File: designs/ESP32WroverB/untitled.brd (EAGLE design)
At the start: 37 x 48 mm, 19 parts, among them IC6 ESP32-WROVER-B

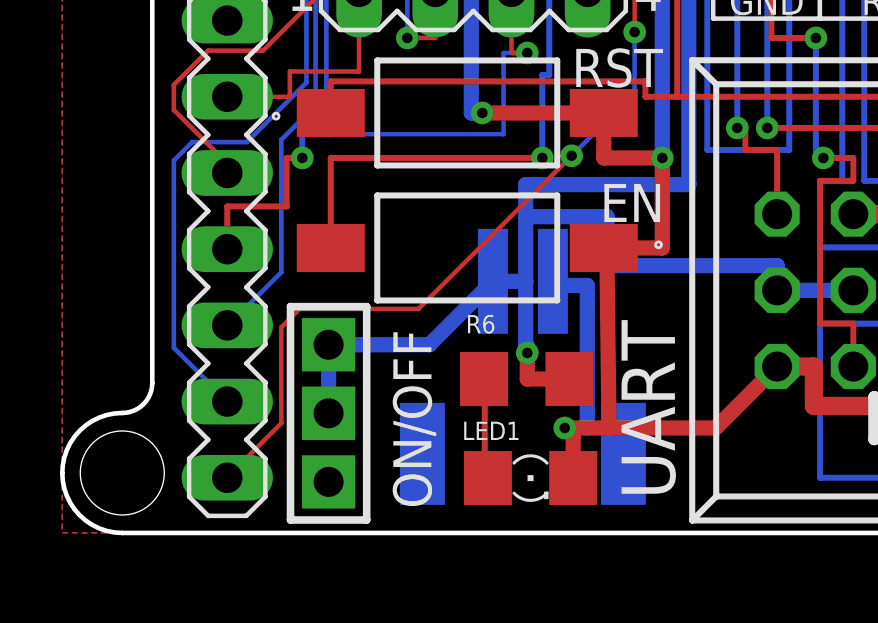
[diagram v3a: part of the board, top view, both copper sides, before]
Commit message: corrected ESP32 on/off error
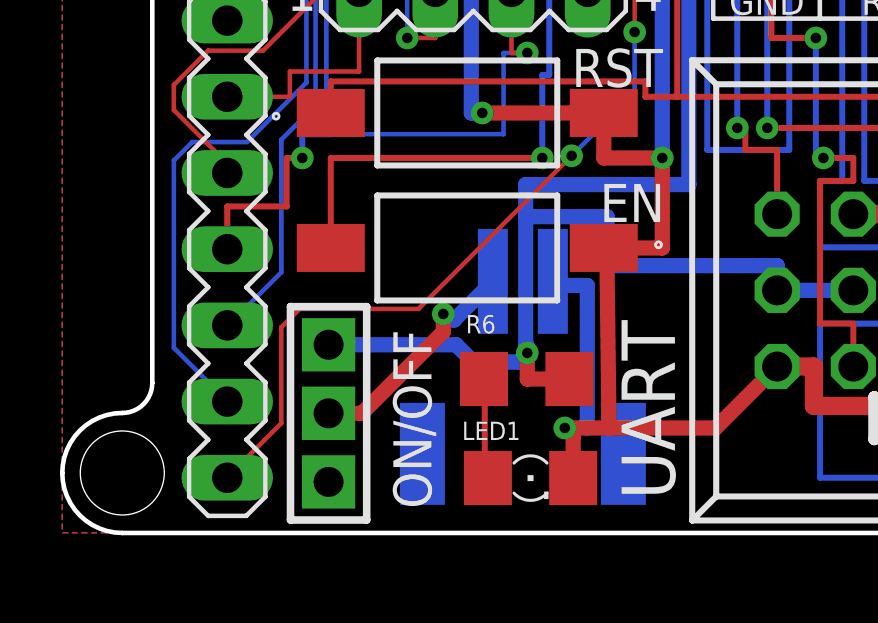
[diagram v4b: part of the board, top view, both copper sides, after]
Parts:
- C1, C4: value (none) -> 1nF
- C2: value (none) -> 100uF
- C3: value (none) -> 1uF
- R1: value 10k -> 12k
- R2: value (none) -> 460ohm
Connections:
- new net N$1: ON/OFF.P$2, POWER.2
- net 3.3V: no longer ON/OFF.P$2, POWER.2
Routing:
- net N$1: track 0.00 -> 7.87 mm, vias 0 -> 1
- net 3.3V: track 99.3 -> 96.6 mm
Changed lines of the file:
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@@
 </autorouter>
 <elements>
-<element name="C1" library="CommonParts" package="C0805" package3d_urn="urn:adsk.eagle:package:23617/2" value="" x="12.584" y="34.087" smashed="yes" rot="MR0">
+<element name="C1" library="CommonParts" package="C0805" package3d_urn="urn:adsk.eagle:package:23617/2" value="1nF" x="12.584" y="34.087" smashed="yes" rot="MR0">
 <attribute name="NAME" x="15.124" y="32.817" size="1.27" layer="26" rot="MR180"/>
 <attribute name="POPULARITY" value="88" x="-2.656" y="-14.173" size="1.778" layer="28" rot="MR0" display="off"/>
@@
 <attribute name="VALUE" x="13.854" y="31.547" size="1.27" layer="28" rot="MR0"/>
 </element>
-<element name="C2" library="CommonParts" package="C0805" package3d_urn="urn:adsk.eagle:package:23617/2" value="" x="12.584" y="31.547" smashed="yes" rot="MR0">
+<element name="C2" library="CommonParts" package="C0805" package3d_urn="urn:adsk.eagle:package:23617/2" value="100uF" x="12.584" y="31.547" smashed="yes" rot="MR0">
 <attribute name="NAME" x="15.124" y="30.277" size="1.27" layer="26" rot="MR180"/>
 <attribute name="POPULARITY" value="88" x="-7.736" y="-16.713" size="1.778" layer="28" rot="MR0" display="off"/>
@@
 <attribute name="VALUE" x="13.854" y="29.007" size="1.27" layer="28" rot="MR0"/>
 </element>
-<element name="C3" library="CommonParts" package="C0805" package3d_urn="urn:adsk.eagle:package:23617/2" value="" x="12.584" y="29.007" smashed="yes" rot="MR0">
+<element name="C3" library="CommonParts" package="C0805" package3d_urn="urn:adsk.eagle:package:23617/2" value="1uF" x="12.584" y="29.007" smashed="yes" rot="MR0">
 <attribute name="NAME" x="15.124" y="27.737" size="1.27" layer="26" rot="MR180"/>
 <attribute name="POPULARITY" value="88" x="-12.816" y="-19.253" size="1.778" layer="28" rot="MR0" display="off"/>
@@
 <attribute name="VALUE" x="13.854" y="26.467" size="1.27" layer="28" rot="MR0"/>
 </element>
-<element name="C4" library="CommonParts" package="C0805" package3d_urn="urn:adsk.eagle:package:23617/2" value="" x="12.584" y="26.467" smashed="yes" rot="MR0">
+<element name="C4" library="CommonParts" package="C0805" package3d_urn="urn:adsk.eagle:package:23617/2" value="1nF" x="12.584" y="26.467" smashed="yes" rot="MR0">
 <attribute name="NAME" x="15.124" y="25.197" size="1.27" layer="26" rot="MR180"/>
 <attribute name="POPULARITY" value="88" x="-17.896" y="-21.793" size="1.778" layer="28" rot="MR0" display="off"/>
@@
 <attribute name="PRICE" value="None" x="59.074" y="13.467" size="1.778" layer="28" rot="MR180" display="off"/>
 </element>
-<element name="R1" library="CommonParts" package="R0805" package3d_urn="urn:adsk.eagle:package:23553/2" value="10k" x="19.704" y="29.007" smashed="yes" rot="MR0">
+<element name="R1" library="CommonParts" package="R0805" package3d_urn="urn:adsk.eagle:package:23553/2" value="12k" x="19.704" y="29.007" smashed="yes" rot="MR0">
 <attribute name="NAME" x="22.879" y="29.007" size="1.27" layer="26" rot="MR180"/>
 </element>
-<element name="R2" library="CommonParts" package="R0805" package3d_urn="urn:adsk.eagle:package:23553/2" value="" x="19.704" y="26.467" smashed="yes" rot="MR180">
+<element name="R2" library="CommonParts" package="R0805" package3d_urn="urn:adsk.eagle:package:23553/2" value="460ohm" x="19.704" y="26.467" smashed="yes" rot="MR180">
 <attribute name="NAME" x="22.879" y="26.467" size="1.27" layer="26" rot="MR180"/>
 <attribute name="VALUE" x="19.069" y="29.007" size="1.27" layer="28" rot="MR180"/>
@@
 <contactref element="ON/OFF" pad="P$1"/>
 <contactref element="R6" pad="2"/>
-<contactref element="POWER" pad="2"/>
-<contactref element="ON/OFF" pad="P$2"/>
 <contactref element="UART" pad="3"/>
 <contactref element="UART" pad="4"/>
 <contactref element="SV5" pad="8"/>
-<wire x1="10.241" y1="6.274" x2="12.354" y2="8.387" width="0.508" layer="16"/>
-<wire x1="10.241" y1="6.274" x2="6.877" y2="6.274" width="0.508" layer="16"/>
-<wire x1="6.877" y1="3.988" x2="6.877" y2="6.274" width="0.508" layer="16"/>
 <wire x1="3.5" y1="42.62" x2="6.402" y2="45.522" width="0.508" layer="1"/>
 <wire x1="6.402" y1="45.522" x2="8.65" y2="45.522" width="0.508" layer="1"/>
@@
 <wire x1="13.5" y1="6" x2="13.5" y2="6.2306" width="0.508" layer="16"/>
 <wire x1="13.5" y1="6.2306" x2="13.4476" y2="6.2306" width="0.508" layer="16"/>
-<wire x1="12.354" y1="8.387" x2="13.4476" y2="8.387" width="0.508" layer="16"/>
-<wire x1="13.4476" y1="6.2306" x2="13.4476" y2="8.387" width="0.508" layer="16"/>
-<wire x1="13.4476" y1="8.387" x2="13.4476" y2="10.5434" width="0.508" layer="16"/>
+<wire x1="13.4476" y1="6.2306" x2="13.4476" y2="10.5434" width="0.508" layer="16"/>
 <wire x1="16.1604" y1="10.5434" x2="16.1604" y2="8.9104" width="0.508" layer="16"/>
 <wire x1="16.1604" y1="8.9104" x2="21.828" y2="8.9104" width="0.508" layer="16"/>
@@
 <wire x1="14.5904" y1="27.6234" x2="13.534" y2="27.6234" width="0.508" layer="16"/>
 <wire x1="13.534" y1="27.6234" x2="13.534" y2="29.007" width="0.508" layer="16"/>
+<wire x1="11.126" y1="6.274" x2="11.7" y2="5.7" width="0.508" layer="16"/>
+<wire x1="11.7" y1="5.7" x2="13.2" y2="5.7" width="0.508" layer="16"/>
+<wire x1="13.2" y1="5.7" x2="13.5" y2="6" width="0.508" layer="16"/>
+<wire x1="6.877" y1="6.274" x2="11.126" y2="6.274" width="0.508" layer="16"/>
 </signal>
 <signal name="RXD0" class="1">
@@
 <contactref element="SV1" pad="6"/>
 </signal>
+<signal name="N$1">
+<contactref element="POWER" pad="2"/>
+<contactref element="ON/OFF" pad="P$2"/>
+<wire x1="12.354" y1="8.387" x2="11.067" y2="7.1" width="0.508" layer="16"/>
+<wire x1="11.067" y1="7.1" x2="10.8" y2="7.1" width="0.508" layer="16"/>
+<wire x1="10.8" y1="7.1" x2="10.7" y2="7.2" width="0.508" layer="16"/>
+<wire x1="10.7" y1="7.2" x2="10.7" y2="7.3" width="0.508" layer="16"/>
+<via x="10.7" y="7.3" extent="1-16" drill="0.35"/>
+<wire x1="10.7" y1="7.3" x2="10.7" y2="6.7" width="0.508" layer="1"/>
+<wire x1="7.988" y1="3.988" x2="6.877" y2="3.988" width="0.508" layer="1"/>
+<wire x1="10.7" y1="6.7" x2="7.988" y2="3.988" width="0.508" layer="1"/>
+</signal>
 </signals>

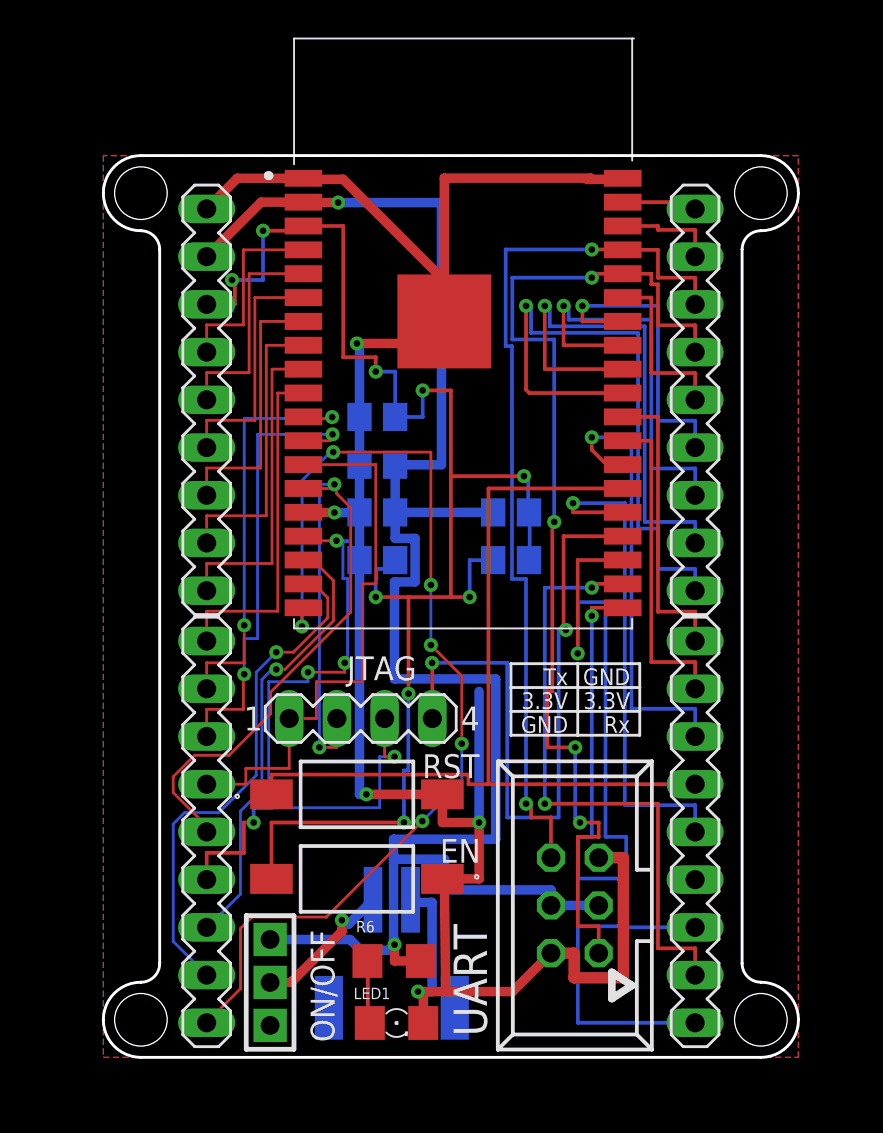
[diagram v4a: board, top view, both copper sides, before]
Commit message: changed 1206 100uF Capacitor
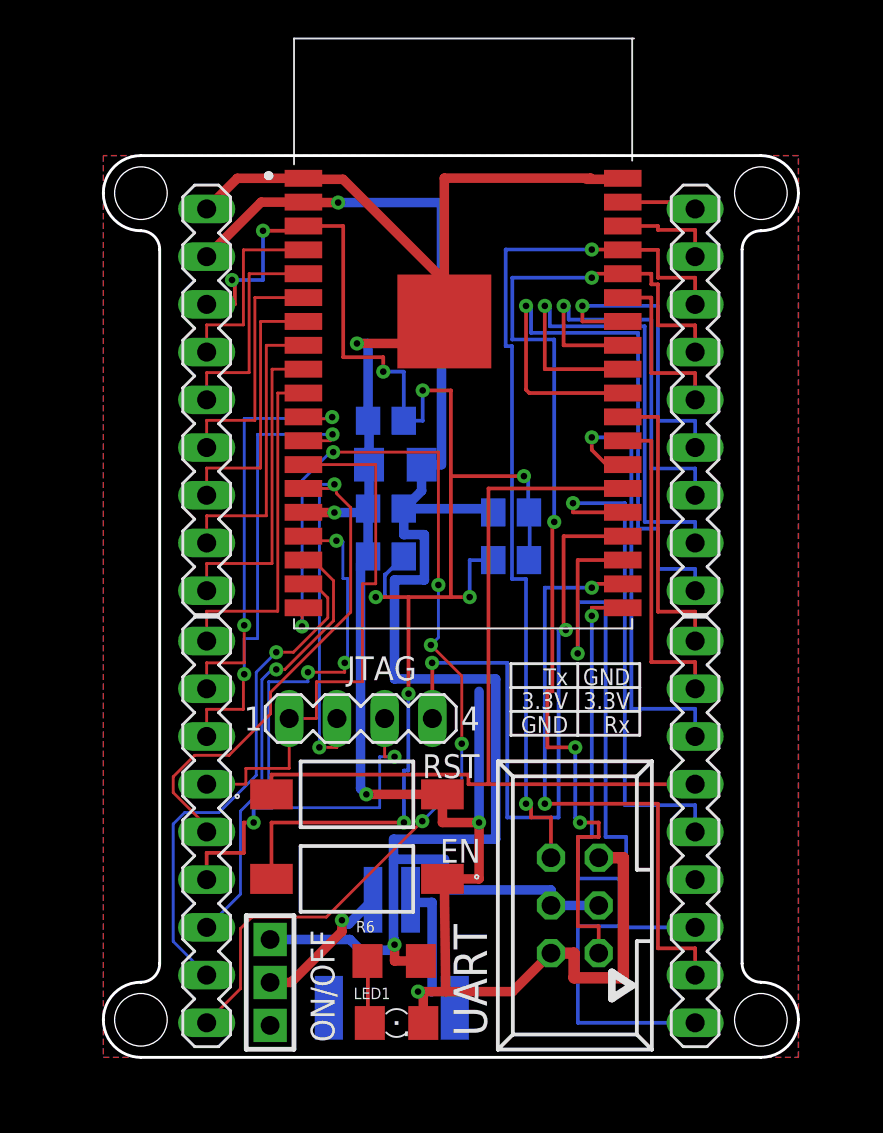
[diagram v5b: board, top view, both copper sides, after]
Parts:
- C2: device CommonParts:C0805 -> CommonParts:C1206
- moved C2 0.96 mm to (13.5, 31.5)
- moved C1 0.50 mm to (13.0, 33.9)
- moved C4 0.50 mm to (13.0, 26.7)
- moved C3 0.50 mm to (13.0, 29.2)
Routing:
- net GND: track 120.2 -> 121.3 mm
- net 3.3V: track 96.6 -> 95.7 mm
- net CMD: track 55.5 -> 56.1 mm
- net GPIO13: track 40.8 -> 40.3 mm

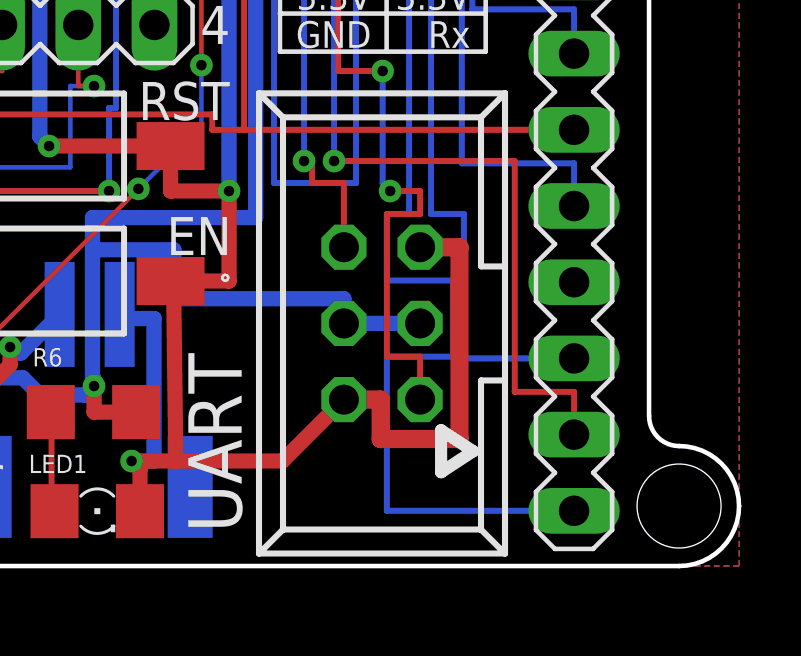
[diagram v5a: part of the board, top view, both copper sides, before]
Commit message: numitron 4 resistor error correction
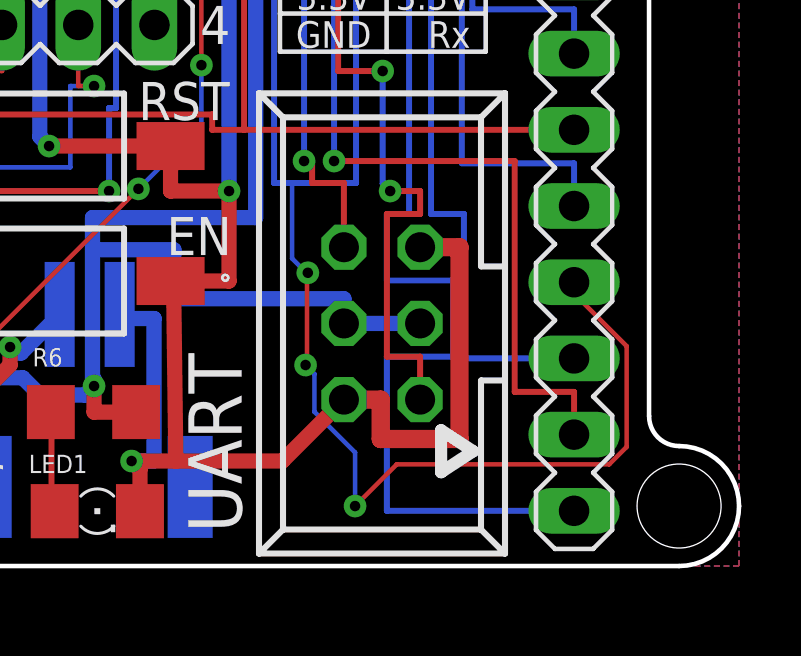
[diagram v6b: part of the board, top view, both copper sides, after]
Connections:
- removed net IO15: SV1.6
- net GPIO15: now also SV1.6
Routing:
- net GPIO15: track 36.6 -> 64.4 mm, vias 2 -> 5
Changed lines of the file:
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@@
 <wire x1="22.6194" y1="22.75" x2="22.2322" y2="22.75" width="0.2" layer="16"/>
 <wire x1="22.2322" y1="22.75" x2="22.2322" y2="12.7678" width="0.2" layer="16"/>
-<wire x1="22.2322" y1="12.7678" x2="19.5" y2="12.7678" width="0.2" layer="16"/>
+<wire x1="22.2322" y1="12.7678" x2="20.1" y2="12.7678" width="0.2" layer="16"/>
+<wire x1="20.1" y1="12.7678" x2="19.5" y2="12.7678" width="0.2" layer="16"/>
 <wire x1="19.5" y1="12.7678" x2="19.5" y2="21" width="0.2" layer="16"/>
 <wire x1="19.5" y1="21" x2="15.5" y2="21" width="0.2" layer="16"/>
@@
 <wire x1="15.5" y1="21" x2="15.513" y2="21" width="0.2" layer="1"/>
 <wire x1="15.513" y1="21" x2="15.513" y2="18.037" width="0.2" layer="1"/>
+<contactref element="SV1" pad="6"/>
+<wire x1="20.1" y1="12.7678" x2="20.1" y2="10.25" width="0.1524" layer="16"/>
+<wire x1="20.1" y1="10.25" x2="20.6" y2="9.75" width="0.1524" layer="16"/>
+<wire x1="20.6" y1="9.75" x2="20.625" y2="9.775" width="0.1524" layer="16"/>
+<via x="20.625" y="9.775" extent="1-16" drill="0.35"/>
+<wire x1="20.625" y1="9.775" x2="20.6" y2="9.75" width="0.1524" layer="1"/>
+<wire x1="20.6" y1="9.75" x2="20.6" y2="6.75" width="0.1524" layer="1"/>
+<wire x1="20.6" y1="6.75" x2="20.55" y2="6.7" width="0.1524" layer="1"/>
+<via x="20.55" y="6.7" extent="1-16" drill="0.35"/>
+<wire x1="20.55" y1="6.7" x2="20.8454" y2="6.4046" width="0.1524" layer="16"/>
+<wire x1="22.2" y1="3.78539375" x2="22.2" y2="2" width="0.1524" layer="16"/>
+<wire x1="20.8454" y1="6.4046" x2="20.8454" y2="5.13999375" width="0.1524" layer="16"/>
+<wire x1="20.8454" y1="5.13999375" x2="22.2" y2="3.78539375" width="0.1524" layer="16"/>
+<via x="22.2" y="2" extent="1-16" drill="0.35"/>
+<wire x1="30.672325" y1="3.3894" x2="31.2526" y2="3.969675" width="0.1524" layer="1"/>
+<wire x1="31.2526" y1="3.969675" x2="31.2526" y2="7.330325" width="0.1524" layer="1"/>
+<wire x1="31.2526" y1="7.330325" x2="29.5" y2="9.082925" width="0.1524" layer="1"/>
+<wire x1="22.2" y1="2" x2="23.5894" y2="3.3894" width="0.1524" layer="1"/>
+<wire x1="23.5894" y1="3.3894" x2="30.672325" y2="3.3894" width="0.1524" layer="1"/>
+<wire x1="29.5" y1="9.082925" x2="29.5" y2="9.46" width="0.1524" layer="1"/>
 </signal>
 <signal name="SEN_VP">
@@
 <wire x1="29.5" y1="45.522" x2="29.5" y2="45.16" width="0.2" layer="1"/>
 </signal>
-<signal name="IO15">
-<contactref element="SV1" pad="6"/>
-</signal>
 <signal name="N$1">
